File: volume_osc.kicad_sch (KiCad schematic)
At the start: 19 parts, among them Q6 2N3904, Q7 2N3904, Q8 2N3904

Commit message: Placed in smd and through.
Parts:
- C13, C17, C18: footprint Capacitor_THT:CP_Radial_D10.0mm_P3.80mm -> Capacitor_THT:CP_Radial_D5.0mm_P2.50mm
- C14, C15, C16: footprint Capacitor_THT:C_Disc_D11.0mm_W5.0mm_P7.50mm -> Capacitor_SMD:C_0805_2012Metric
- L11: footprint Inductor_THT:L_Axial_L7.0mm_D3.3mm_P12.70mm_Horizontal_Fastron_MICC -> Inductor_SMD:L_1210_3225Metric
- R15, R16, R17, R18, R19, R20, R21, R22, R40: footprint Resistor_THT:R_Axial_DIN0207_L6.3mm_D2.5mm_P10.16mm_Horizontal -> Resistor_SMD:R_0805_2012Metric
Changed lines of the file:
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@@
       (effects (font (size 1.27 1.27)) (justify left))
     )
-    (property "Footprint" "Inductor_THT:L_Axial_L7.0mm_D3.3mm_P12.70mm_Horizontal_Fastron_MICC" (at 82.55 58.42 0)
+    (property "Footprint" "Inductor_SMD:L_1210_3225Metric" (at 82.55 58.42 0)
       (effects (font (size 1.27 1.27)) hide)
     )
@@
       (effects (font (size 1.27 1.27)) (justify left))
     )
-    (property "Footprint" "Capacitor_THT:C_Disc_D11.0mm_W5.0mm_P7.50mm" (at 107.6452 82.55 0)
+    (property "Footprint" "Capacitor_SMD:C_0805_2012Metric" (at 107.6452 82.55 0)
       (effects (font (size 1.27 1.27)) hide)
     )
@@
       (effects (font (size 1.27 1.27)) (justify left))
     )
-    (property "Footprint" "Resistor_THT:R_Axial_DIN0207_L6.3mm_D2.5mm_P10.16mm_Horizontal" (at 168.656 85.344 90)
+    (property "Footprint" "Resistor_SMD:R_0805_2012Metric" (at 168.656 85.344 90)
       (effects (font (size 1.27 1.27)) hide)
     )
@@
       (effects (font (size 1.27 1.27)) (justify right))
     )
-    (property "Footprint" "Resistor_THT:R_Axial_DIN0207_L6.3mm_D2.5mm_P10.16mm_Horizontal" (at 186.944 87.376 90)
+    (property "Footprint" "Resistor_SMD:R_0805_2012Metric" (at 186.944 87.376 90)
       (effects (font (size 1.27 1.27)) hide)
     )
@@
       (effects (font (size 1.27 1.27)))
     )
-    (property "Footprint" "Resistor_THT:R_Axial_DIN0207_L6.3mm_D2.5mm_P10.16mm_Horizontal" (at 178.054 68.834 90)
+    (property "Footprint" "Resistor_SMD:R_0805_2012Metric" (at 178.054 68.834 90)
       (effects (font (size 1.27 1.27)) hide)
     )
@@
       (effects (font (size 1.27 1.27)) (justify left))
     )
-    (property "Footprint" "Resistor_THT:R_Axial_DIN0207_L6.3mm_D2.5mm_P10.16mm_Horizontal" (at 87.376 90.424 90)
+    (property "Footprint" "Resistor_SMD:R_0805_2012Metric" (at 87.376 90.424 90)
       (effects (font (size 1.27 1.27)) hide)
     )
@@
       (effects (font (size 1.27 1.27)) (justify left))
     )
-    (property "Footprint" "Resistor_THT:R_Axial_DIN0207_L6.3mm_D2.5mm_P10.16mm_Horizontal" (at 124.206 81.534 90)
+    (property "Footprint" "Resistor_SMD:R_0805_2012Metric" (at 124.206 81.534 90)
       (effects (font (size 1.27 1.27)) hide)
     )
@@
       (effects (font (size 1.27 1.27)) (justify left))
     )
-    (property "Footprint" "Capacitor_THT:C_Disc_D11.0mm_W5.0mm_P7.50mm" (at 188.9252 68.58 0)
+    (property "Footprint" "Capacitor_SMD:C_0805_2012Metric" (at 188.9252 68.58 0)
       (effects (font (size 1.27 1.27)) hide)
     )
@@
       (effects (font (size 1.27 1.27)) (justify left))
     )
-    (property "Footprint" "Capacitor_THT:C_Disc_D11.0mm_W5.0mm_P7.50mm" (at 107.6452 69.85 0)
+    (property "Footprint" "Capacitor_SMD:C_0805_2012Metric" (at 107.6452 69.85 0)
       (effects (font (size 1.27 1.27)) hide)
     )
@@
       (effects (font (size 1.27 1.27)) (justify left))
     )
-    (property "Footprint" "Resistor_THT:R_Axial_DIN0207_L6.3mm_D2.5mm_P10.16mm_Horizontal" (at 155.956 84.074 90)
+    (property "Footprint" "Resistor_SMD:R_0805_2012Metric" (at 155.956 84.074 90)
       (effects (font (size 1.27 1.27)) hide)
     )
@@
       (effects (font (size 1.27 1.27)))
     )
-    (property "Footprint" "Capacitor_THT:CP_Radial_D10.0mm_P3.80mm" (at 182.88 80.3148 0)
+    (property "Footprint" "Capacitor_THT:CP_Radial_D5.0mm_P2.50mm" (at 182.88 80.3148 0)
       (effects (font (size 1.27 1.27)) hide)
     )
@@
       (effects (font (size 1.27 1.27)) (justify left))
     )
-    (property "Footprint" "Capacitor_THT:CP_Radial_D10.0mm_P3.80mm" (at 51.7652 72.39 0)
+    (property "Footprint" "Capacitor_THT:CP_Radial_D5.0mm_P2.50mm" (at 51.7652 72.39 0)
       (effects (font (size 1.27 1.27)) hide)
     )
@@
       (effects (font (size 1.27 1.27)) (justify right))
     )
-    (property "Footprint" "Resistor_THT:R_Axial_DIN0207_L6.3mm_D2.5mm_P10.16mm_Horizontal" (at 195.834 87.376 90)
+    (property "Footprint" "Resistor_SMD:R_0805_2012Metric" (at 195.834 87.376 90)
       (effects (font (size 1.27 1.27)) hide)
     )
@@
       (effects (font (size 1.27 1.27)) (justify right))
     )
-    (property "Footprint" "Resistor_THT:R_Axial_DIN0207_L6.3mm_D2.5mm_P10.16mm_Horizontal" (at 186.944 74.676 90)
+    (property "Footprint" "Resistor_SMD:R_0805_2012Metric" (at 186.944 74.676 90)
       (effects (font (size 1.27 1.27)) hide)
     )
@@
       (effects (font (size 1.27 1.27)) (justify left))
     )
-    (property "Footprint" "Resistor_THT:R_Axial_DIN0207_L6.3mm_D2.5mm_P10.16mm_Horizontal" (at 70.866 78.994 90)
+    (property "Footprint" "Resistor_SMD:R_0805_2012Metric" (at 70.866 78.994 90)
       (effects (font (size 1.27 1.27)) hide)
     )
@@
       (effects (font (size 1.27 1.27)) (justify left))
     )
-    (property "Footprint" "Capacitor_THT:CP_Radial_D10.0mm_P3.80mm" (at 145.7452 88.9 0)
-      (effects (font (size 1.27 1.27)) hide)
-    )
+    (property "Footprint" "Capacitor_THT:CP_Radial_D5.0mm_P2.50mm" (at 145.7452 88.9 0)
+      (effects (font (size 1.27 1.27)) hide)
+    )

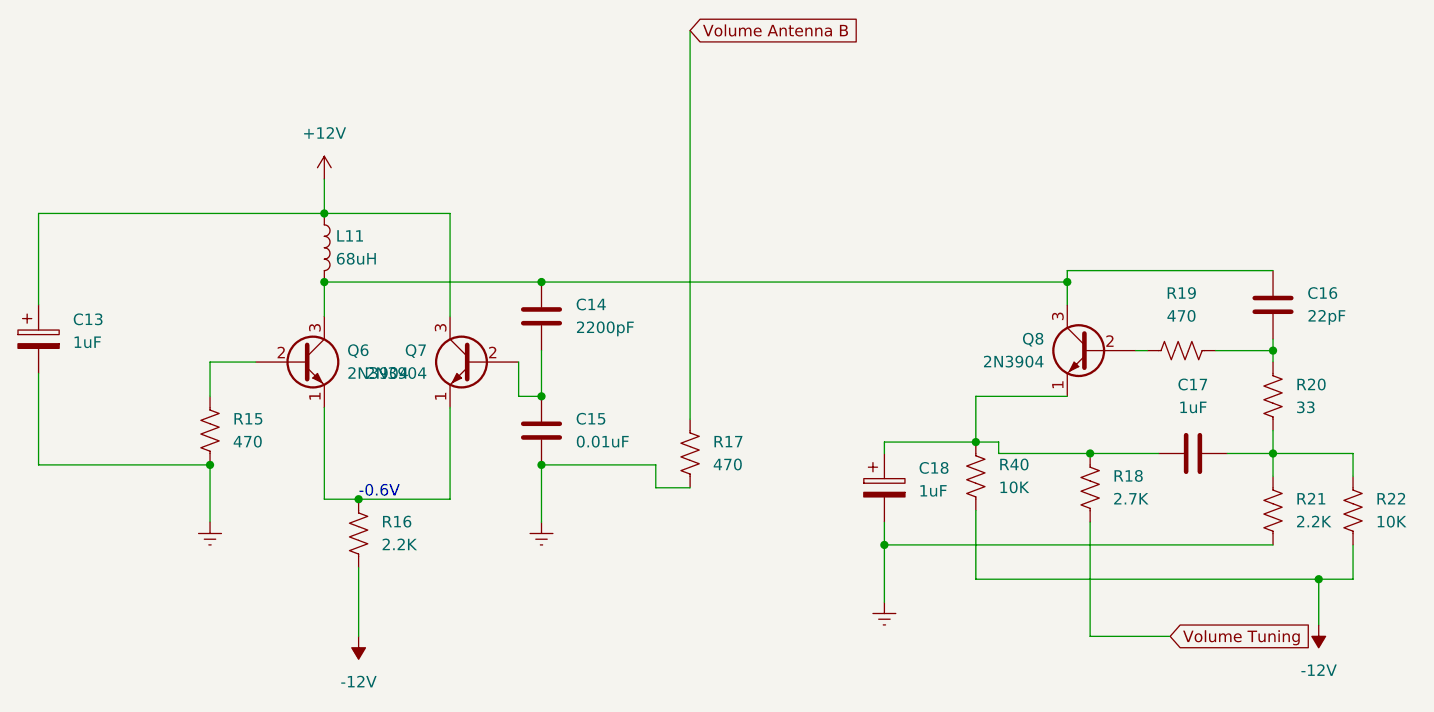
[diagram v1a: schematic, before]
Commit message: Layout cleanup for smd and through
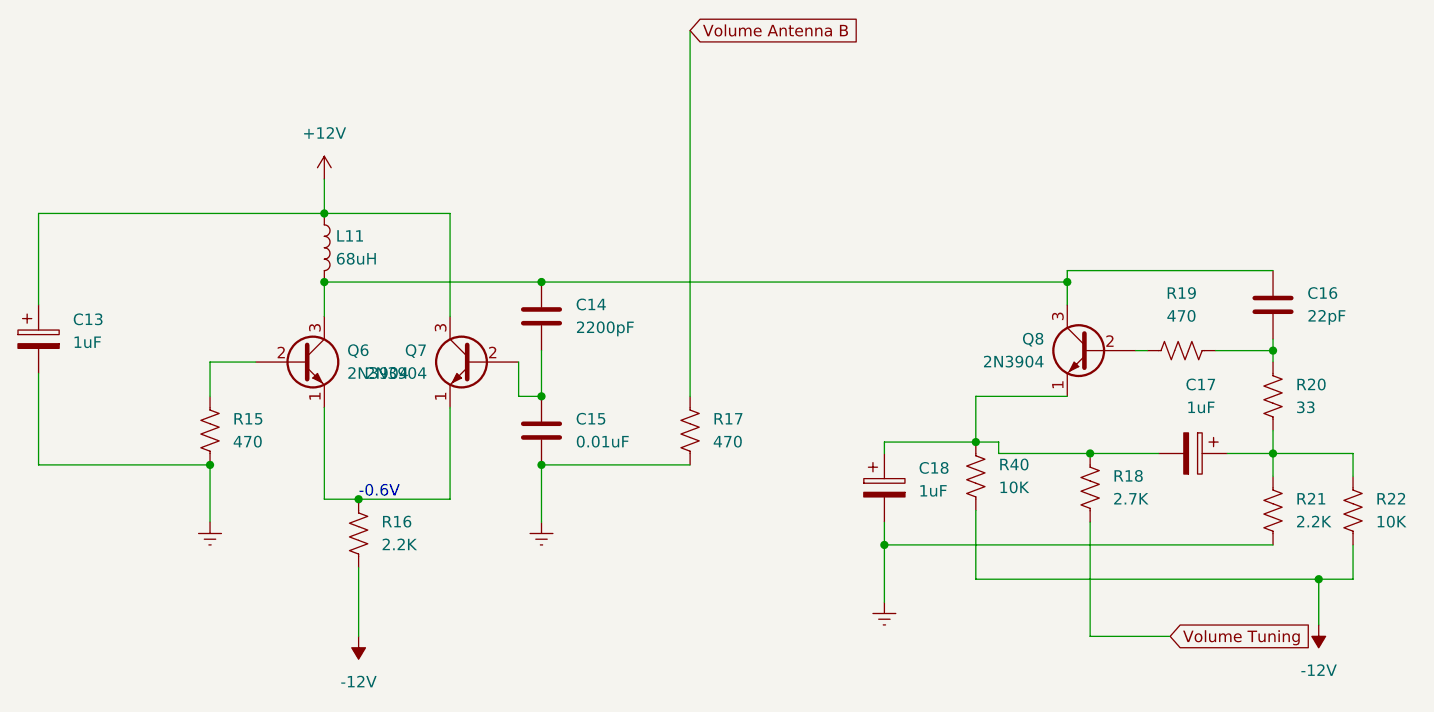
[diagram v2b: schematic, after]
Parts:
- C17: symbol Device:C -> Device:C_Polarized
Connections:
- net at C18.1, Q8.1 (E), R18.1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: now also C17.2; no longer C17.1
- net at R20.1, R21.2, R22.2: now also C17.1; no longer C17.2
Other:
- moved on the sheet: R17
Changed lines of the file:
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@@
     (stroke (width 0) (type default))
   )
-  (wire (pts (xy 106.68 82.55) (xy 119.38 82.55))
+  (wire (pts (xy 106.68 82.55) (xy 123.19 82.55))
     (stroke (width 0) (type default))
   )
@@
     (stroke (width 0) (type default))
   )
-  (wire (pts (xy 123.19 77.47) (xy 123.19 34.29))
+  (wire (pts (xy 123.19 74.93) (xy 123.19 34.29))
     (stroke (width 0) (type default))
   )
@@
     (stroke (width 0) (type default))
   )
-  (wire (pts (xy 119.38 82.55) (xy 119.38 85.09))
-    (stroke (width 0) (type default))
-  )
   (wire (pts (xy 106.68 88.9) (xy 106.68 82.55))
     (stroke (width 0) (type default))
@@
   )
   (wire (pts (xy 82.55 62.23) (xy 106.68 62.23))
-    (stroke (width 0) (type default))
-  )
-  (wire (pts (xy 119.38 85.09) (xy 123.19 85.09))
     (stroke (width 0) (type default))
   )
@@
     )
   )
-  (symbol (lib_id "Device:R_US") (at 123.19 81.28 0) (unit 1)
-    (in_bom yes) (on_board yes) (dnp no) (fields_autoplaced)
-    (property "Reference" "R17" (at 125.73 80.01 0)
-      (effects (font (size 1.27 1.27)) (justify left))
-    )
-    (property "Value" "470" (at 125.73 82.55 0)
-      (effects (font (size 1.27 1.27)) (justify left))
-    )
-    (property "Footprint" "Resistor_SMD:R_0805_2012Metric" (at 124.206 81.534 90)
-      (effects (font (size 1.27 1.27)) hide)
-    )
-    (property "Datasheet" "~" (at 123.19 81.28 0)
+  (symbol (lib_id "Device:R_US") (at 123.19 78.74 0) (unit 1)
+    (in_bom yes) (on_board yes) (dnp no) (fields_autoplaced)
+    (property "Reference" "R17" (at 125.73 77.47 0)
+      (effects (font (size 1.27 1.27)) (justify left))
+    )
+    (property "Value" "470" (at 125.73 80.01 0)
+      (effects (font (size 1.27 1.27)) (justify left))
+    )
+    (property "Footprint" "Resistor_SMD:R_0805_2012Metric" (at 124.206 78.994 90)
+      (effects (font (size 1.27 1.27)) hide)
+    )
+    (property "Datasheet" "~" (at 123.19 78.74 0)
       (effects (font (size 1.27 1.27)) hide)
     )
@@
     )
   )
-  (symbol (lib_id "Device:C") (at 179.07 81.28 90) (unit 1)
-    (in_bom yes) (on_board yes) (dnp no) (fields_autoplaced)
-    (property "Reference" "C17" (at 179.07 73.66 90)
+  (symbol (lib_id "Device:C_Polarized") (at 179.07 81.28 270) (unit 1)
+    (in_bom yes) (on_board yes) (dnp no) (fields_autoplaced)
+    (property "Reference" "C17" (at 179.959 73.66 90)
       (effects (font (size 1.27 1.27)))
     )
-    (property "Value" "1uF" (at 179.07 76.2 90)
+    (property "Value" "1uF" (at 179.959 76.2 90)
       (effects (font (size 1.27 1.27)))
     )
-    (property "Footprint" "Capacitor_THT:CP_Radial_D5.0mm_P2.50mm" (at 182.88 80.3148 0)
-      (effects (font (size 1.27 1.27)) hide)
-    )
+    (property "Footprint" "Capacitor_THT:CP_Radial_D5.0mm_P2.50mm" (at 175.26 82.2452 0)
+      (effects (font (size 1.27 1.27)) hide)
+    )
